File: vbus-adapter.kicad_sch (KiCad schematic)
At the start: 32 parts, among them J1 VBUS, J2 CAN, J3 Screw_Terminal_01x03, J4 Screw_Terminal_01x03, J6 Backup GPIO, T800 AO3400A, U1 ISO7721D, U3 MCP2562-E-SN, U4 WeMos_S2_mini

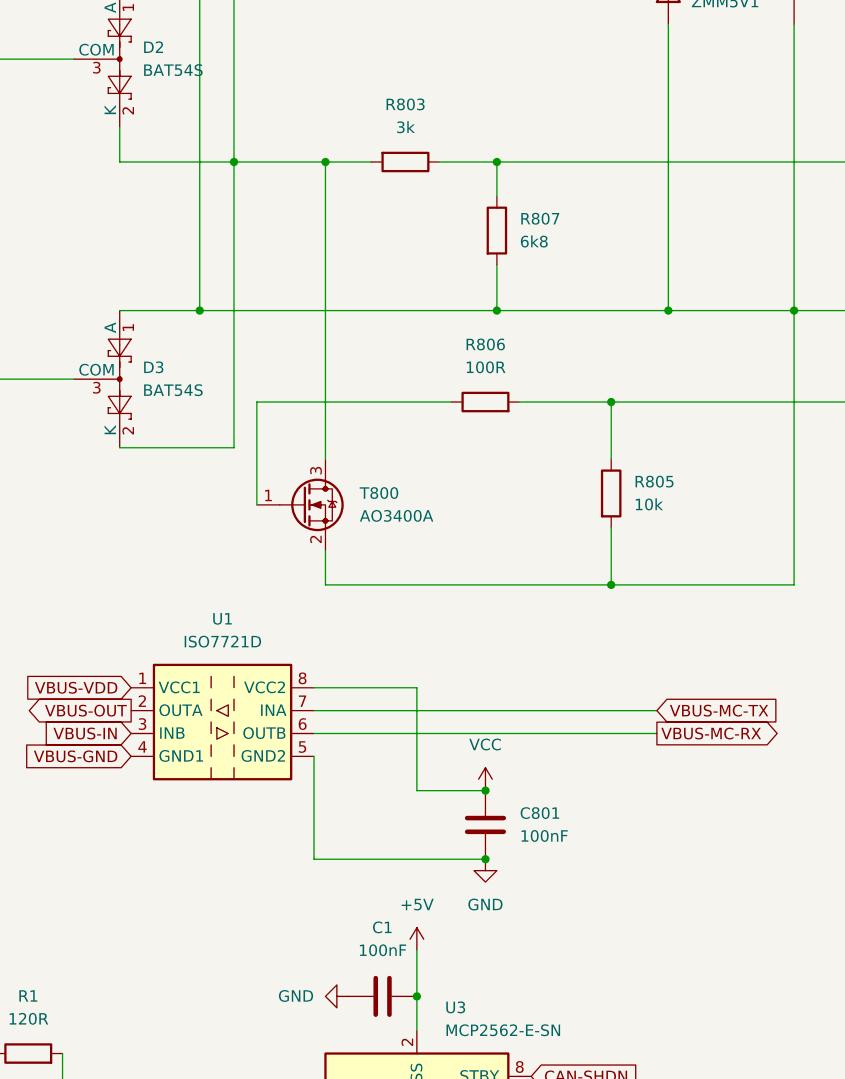
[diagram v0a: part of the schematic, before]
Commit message: Fix some issues
- Use ISO7721FDR (Default Low output) so on disconnect of
  the ESP32 (Power loss) the VBUS will not be pulled to low
  e.g. bus disabled.
- Add pull-down resistor to ISO input for TX
- Add VBUS r/w jumper disconnecting the MOSFet drain from the VBUS
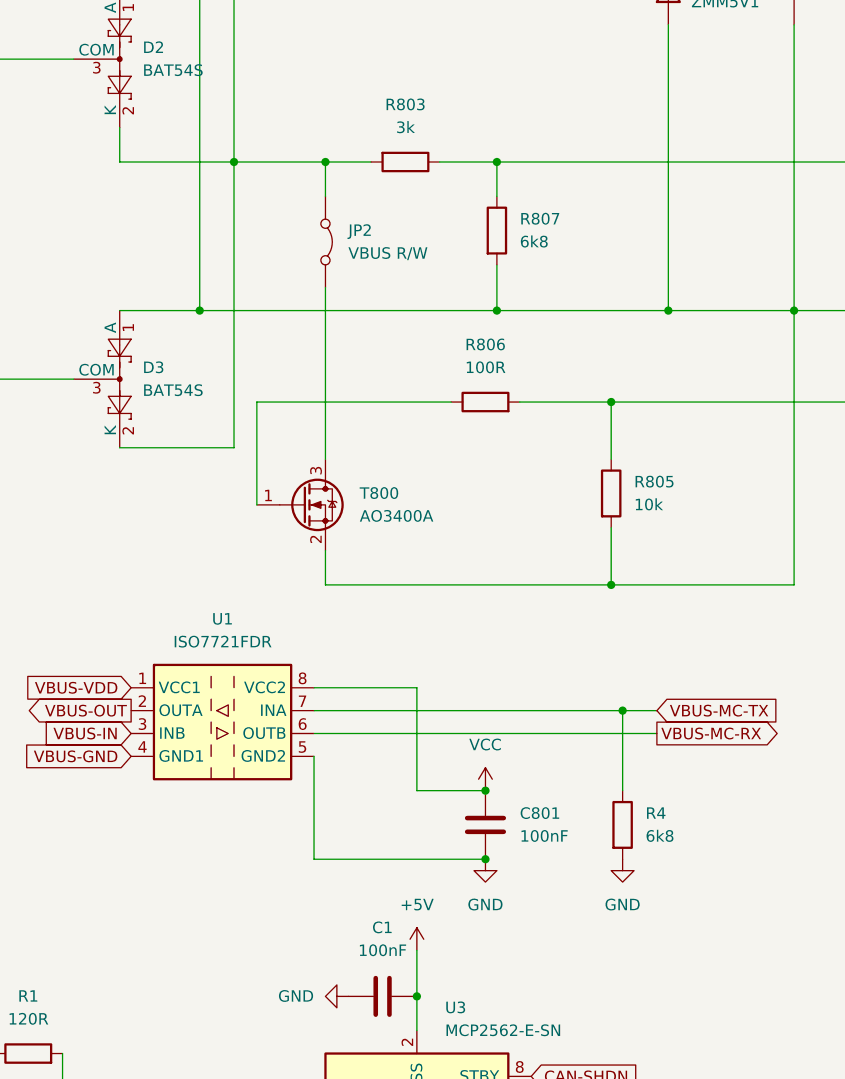
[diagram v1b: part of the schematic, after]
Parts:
- added JP2: VBUS R/W, Connector_PinHeader_2.54mm:PinHeader_1x02_P2.54mm_Vertical, symbol Jumper:Jumper_2_Bridged
- added R4: 6k8, Resistor_SMD:R_0805_2012Metric_Pad1.20x1.40mm_HandSolder, symbol Device:R
- U1: value ISO7721D -> ISO7721FDR
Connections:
- net GND: now also R4.2
- net VBUS-MC-TX: now also R4.1
- net at D2.2 (K), D3.2 (K), D4.3 (COM)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: now also JP2.1 (A); no longer T800.3 (D)
- new net: JP2.2 (B), T800.3 (D)
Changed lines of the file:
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@@
 	)
 	(junction
+		(at 137.16 119.38)
+		(diameter 0)
+		(color 0 0 0 0)
+	)
+	(junction
 		(at 54.61 162.56)
 		(diameter 0)
@@
 	(wire
 		(pts
+			(xy 104.14 72.39) (xy 104.14 91.44)
+		)
+		(stroke
+			(width 0)
+			(type default)
+		)
+	)
+	(wire
+		(pts
 			(xy 104.14 58.42) (xy 109.22 58.42)
 		)
@@
 	(wire
 		(pts
+			(xy 137.16 119.38) (xy 140.97 119.38)
+		)
+		(stroke
+			(width 0)
+			(type default)
+		)
+	)
+	(wire
+		(pts
 			(xy 171.45 43.18) (xy 171.45 74.93)
 		)
@@
 	(wire
 		(pts
-			(xy 104.14 58.42) (xy 104.14 91.44)
+			(xy 104.14 58.42) (xy 104.14 62.23)
 		)
 		(stroke
@@
 	(wire
 		(pts
+			(xy 137.16 128.27) (xy 137.16 119.38)
+		)
+		(stroke
+			(width 0)
+			(type default)
+		)
+	)
+	(wire
+		(pts
 			(xy 156.21 29.21) (xy 171.45 29.21)
 		)
@@
 	(wire
 		(pts
-			(xy 102.87 119.38) (xy 140.97 119.38)
+			(xy 102.87 119.38) (xy 137.16 119.38)
 		)
 		(stroke
@@
 	)
 	(symbol
+		(lib_id "power:GND")
+		(at 137.16 135.89 0)
+		(unit 1)
+		(exclude_from_sim no)
+		(in_bom yes)
+		(on_board yes)
+		(dnp no)
+		(fields_autoplaced yes)
+		(property "Reference" "#PWR015"
+			(at 137.16 142.24 0)
+			(effects
+				(font
+					(size 1.27 1.27)
+				)
+				(hide yes)
+			)
+		)
+		(property "Value" "GND"
+			(at 137.16 140.97 0)
+			(effects
+				(font
+					(size 1.27 1.27)
+				)
+			)
+		)
+		(property "Footprint" ""
+			(at 137.16 135.89 0)
+			(effects
+				(font
+					(size 1.27 1.27)
+				)
+				(hide yes)
+			)
+		)
+		(property "Datasheet" ""
+			(at 137.16 135.89 0)
+			(effects
+				(font
+					(size 1.27 1.27)
+				)
+				(hide yes)
+			)
+		)
+		(property "Description" "Power symbol creates a global label with name \"GND\" , ground"
+			(at 137.16 135.89 0)
+			(effects
+				(font
+					(size 1.27 1.27)
+				)
+				(hide yes)
+			)
+		)
+		(pin "1"
+		)
+		(instances
+			(project "vbus-adapter"
+				(path "/c5b76d16-c954-491e-a7b2-87b879d4d4be"
+					(reference "#PWR015")
+					(unit 1)
+				)
+			)
+		)
+	)
+	(symbol
 		(lib_id "Diode:SMAJ12CA")
 		(at 55.88 63.5 270)
@@
 			)
 		)
-		(property "Value" "ISO7721D"
+		(property "Value" "ISO7721FDR"
 			(at 92.71 111.76 0)
 			(effects
@@
 	)
 	(symbol
+		(lib_id "Jumper:Jumper_2_Bridged")
+		(at 104.14 67.31 270)
+		(unit 1)
+		(exclude_from_sim no)
+		(in_bom yes)
+		(on_board yes)
+		(dnp no)
+		(fields_autoplaced yes)
+		(property "Reference" "JP2"
+			(at 106.68 66.0399 90)
+			(effects
+				(font
+					(size 1.27 1.27)
+				)
+				(justify left)
+			)
+		)
+		(property "Value" "VBUS R/W"
+			(at 106.68 68.5799 90)
+			(effects
+				(font
+					(size 1.27 1.27)
+				)
+				(justify left)
+			)
+		)
+		(property "Footprint" "Connector_PinHeader_2.54mm:PinHeader_1x02_P2.54mm_Vertical"
+			(at 104.14 67.31 0)
+			(effects
+				(font
+					(size 1.27 1.27)
+				)
+				(hide yes)
+			)
+		)
+		(property "Datasheet" "~"
+			(at 104.14 67.31 0)
+			(effects
+				(font
+					(size 1.27 1.27)
+				)
+				(hide yes)
+			)
+		)
+		(property "Description" "Jumper, 2-pole, closed/bridged"
+			(at 104.14 67.31 0)
+			(effects
+				(font
+					(size 1.27 1.27)
+				)
+				(hide yes)
+			)
+		)
+		(pin "2"
+		)
+		(pin "1"
+		)
+		(instances
+			(project "vbus-adapter"
+				(path "/c5b76d16-c954-491e-a7b2-87b879d4d4be"
+					(reference "JP2")
+					(unit 1)
+				)
+			)
+		)
+	)
+	(symbol
 		(lib_id "Diode:BAT54S")
 		(at 101.6 21.59 270)
@@
 					(unit 1)
 				)
+			)
+		)
+	)
+	(symbol
+		(lib_id "Device:R")
+		(at 137.16 132.08 0)
+		(unit 1)
+		(exclude_from_sim no)
+		(in_bom yes)
+		(on_board yes)
+		(dnp no)
+		(fields_autoplaced yes)
+		(property "Reference" "R4"
+			(at 139.7 130.8099 0)
+			(effects
+				(font
+					(size 1.27 1.27)
+				)
+				(justify left)
+			)
+		)
+		(property "Value" "6k8"
+			(at 139.7 133.3499 0)
+			(effects
+				(font
+					(size 1.27 1.27)
+				)
+				(justify left)
+			)
+		)
+		(property "Footprint" "Resistor_SMD:R_0805_2012Metric_Pad1.20x1.40mm_HandSolder"
+			(at 135.382 132.08 90)
+			(effects
+				(font
+					(size 1.27 1.27)
+				)
+				(hide yes)
+			)
+		)
+		(property "Datasheet" "~"
+			(at 137.16 132.08 0)
+			(effects
+				(font
+					(size 1.27 1.27)
+				)
+				(hide yes)
+			)
+		)
+		(property "Description" "Resistor"
+			(at 137.16 132.08 0)
+			(effects
+				(font
+					(size 1.27 1.27)
+				)
+				(hide yes)
+			)
+		)
+		(pin "2"
+		)
+		(pin "1"
+		)
+		(instances
+			(project "vbus-adapter"
+				(path "/c5b76d16-c954-491e-a7b2-87b879d4d4be"
+					(reference "R4")
+					(unit 1)
+				)

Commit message: Version 2
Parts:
- removed U4: WeMos_S2_mini, flo:WEMOS_S2_mini, symbol WEMOS_S2_mini:WeMos_S2_mini
- added C3, C6: 10uF, Capacitor_SMD:C_0805_2012Metric_Pad1.18x1.45mm_HandSolder, symbol Device:C_Polarized
- added C4, C5: 0.1uF, Capacitor_SMD:C_0805_2012Metric_Pad1.18x1.45mm_HandSolder, symbol Device:C
- added C7: 10nF, Capacitor_SMD:C_0805_2012Metric_Pad1.18x1.45mm_HandSolder, symbol Device:C
- added J5: Power, TerminalBlock_Phoenix:TerminalBlock_Phoenix_MPT-0,5-2-2.54_1x02_P2.54mm_Horizontal, symbol Connector:Screw_Terminal_01x02
- added J7: Program, Connector_PinHeader_2.54mm:PinHeader_1x05_P2.54mm_Vertical, symbol Connector:Conn_01x05_Pin
- added Q1, Q2: SS8050, Package_TO_SOT_SMD:SOT-23, symbol Transistor_BJT:SS8050
- added R5, R6: 10K, Resistor_SMD:R_0805_2012Metric_Pad1.20x1.40mm_HandSolder, symbol Device:R
- added U2: ESP32-S2-SOLO, PCM_Espressif:ESP32-S2-SOLO, symbol PCM_Espressif:ESP32-S2-SOLO
- added U5: SPX3819M5-L-3-3, Package_TO_SOT_SMD:SOT-23-5, symbol Regulator_Linear:SPX3819M5-L-3-3
- J1, J2: footprint TerminalBlock_Phoenix:TerminalBlock_Phoenix_MKDS-1,5-2-5.08_1x02_P5.08mm_Horizontal -> TerminalBlock_Phoenix:TerminalBlock_Phoenix_MPT-0,5-2-2.54_1x02_P2.54mm_Horizontal
- J3: value Screw_Terminal_01x03 -> Sens 2; footprint TerminalBlock_Phoenix:TerminalBlock_Phoenix_MKDS-1,5-3-5.08_1x03_P5.08mm_Horizontal -> TerminalBlock_Phoenix:TerminalBlock_Phoenix_MPT-0,5-3-2.54_1x03_P2.54mm_Horizontal
- J4: value Screw_Terminal_01x03 -> Sens 1; footprint TerminalBlock_Phoenix:TerminalBlock_Phoenix_MKDS-1,5-3-5.08_1x03_P5.08mm_Horizontal -> TerminalBlock_Phoenix:TerminalBlock_Phoenix_MPT-0,5-3-2.54_1x03_P2.54mm_Horizontal
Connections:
- net +5V: now also C3.1, C4.1, J5.1 (Pin_1), U5.1 (IN), U5.3 (EN)
- net CAN-RX: now also U2.12 (GPIO8/TOUCH8/ADC1_CH7)
- net CAN-SHDN: now also U2.4 (GPIO4/TOUCH4/ADC1_CH3)
- net CAN-TX: now also U2.6 (GPIO6/TOUCH6/ADC1_CH5)
- net GND: now also C3.2, C4.2, C5.2, C6.2, C7.2, J5.2 (Pin_2), J7.1 (Pin_1), U2.1 (GND), U2.40 (GND), U2.41 (GND), U5.2 (GND)
- net GPIO-SENS1: now also U2.26 (GPIO45)
- net GPIO-SENS2: now also U2.25 (SPIIO5/GPIO34/FSPICS0)
- net VBUS-MC-RX: now also U2.20 (GPIO12/TOUCH12/ADC2_CH1/FSPICLK/FSPIIO6)
- net VBUS-MC-TX: now also U2.19 (GPIO11/TOUCH11/ADC2_CH0/FSPID/FSPIIO5)
- net VCC: now also C5.1, C6.1, U2.2 (3V3), U5.5 (OUT)
- net GPIO3 renamed EXT4
- net EXT4: now also U2.33 (MTDO/GPIO40/CLK_OUT2)
- net GPIO5 renamed EXT3
- net EXT3: now also U2.32 (MTCK/GPIO39/CLK_OUT3)
- net GPIO7 renamed EXT2
- net EXT2: now also U2.31 (GPIO38/FSPIWP)
- net GPIO9 renamed EXT1
- net EXT1: now also U2.30 (SPIDQS/GPIO37/FSPIQ)
- new net: J7.4 (Pin_4), Q2.2 (E), R6.2
- new net: J7.5 (Pin_5), Q1.2 (E), R5.2
- new net: C7.1, U5.4 (BP)
- new net: Q1.1 (B), R6.1
- new net: Q2.1 (B), R5.1
- new net EN: Q1.3 (C), U2.3 (EN)
- new net PROG: Q2.3 (C), U2.27 (GPIO0)
- new net PROG_RXD: J7.2 (Pin_2), U2.36 (U0RXD/GPIO44/CLK_OUT2)
- new net PROG_TXD: J7.3 (Pin_3), U2.37 (U0TXD/GPIO43/CLK_OUT1)
- no-connect marks 18 -> 23
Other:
- title: (none) -> vbus-adapter

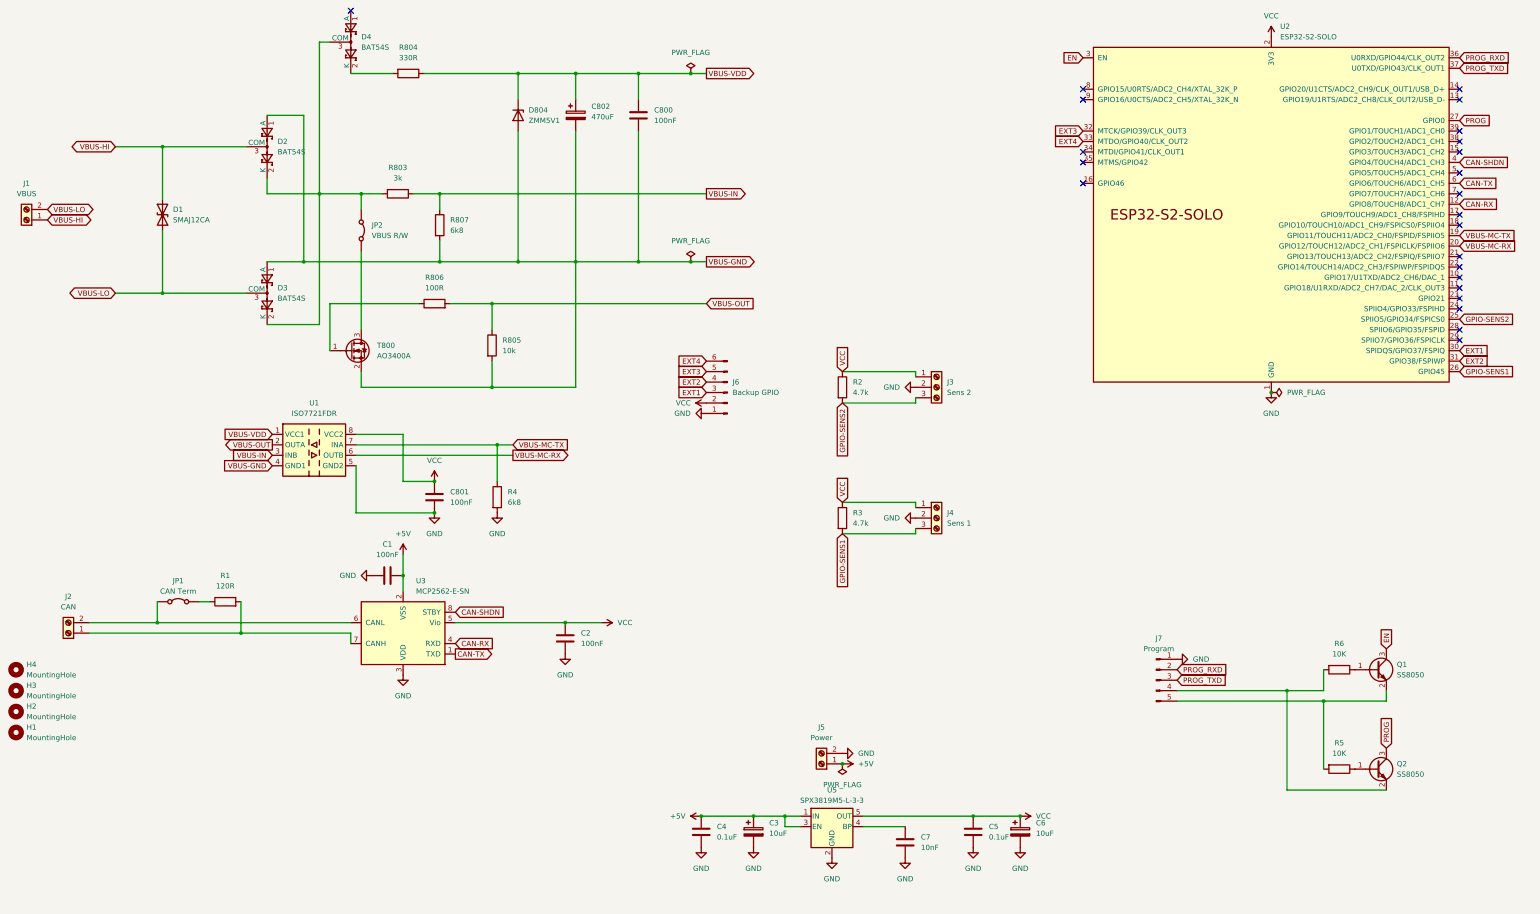
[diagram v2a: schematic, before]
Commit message: Version 3 - Move GPIO for SENS, Add PWR/WIFI LED
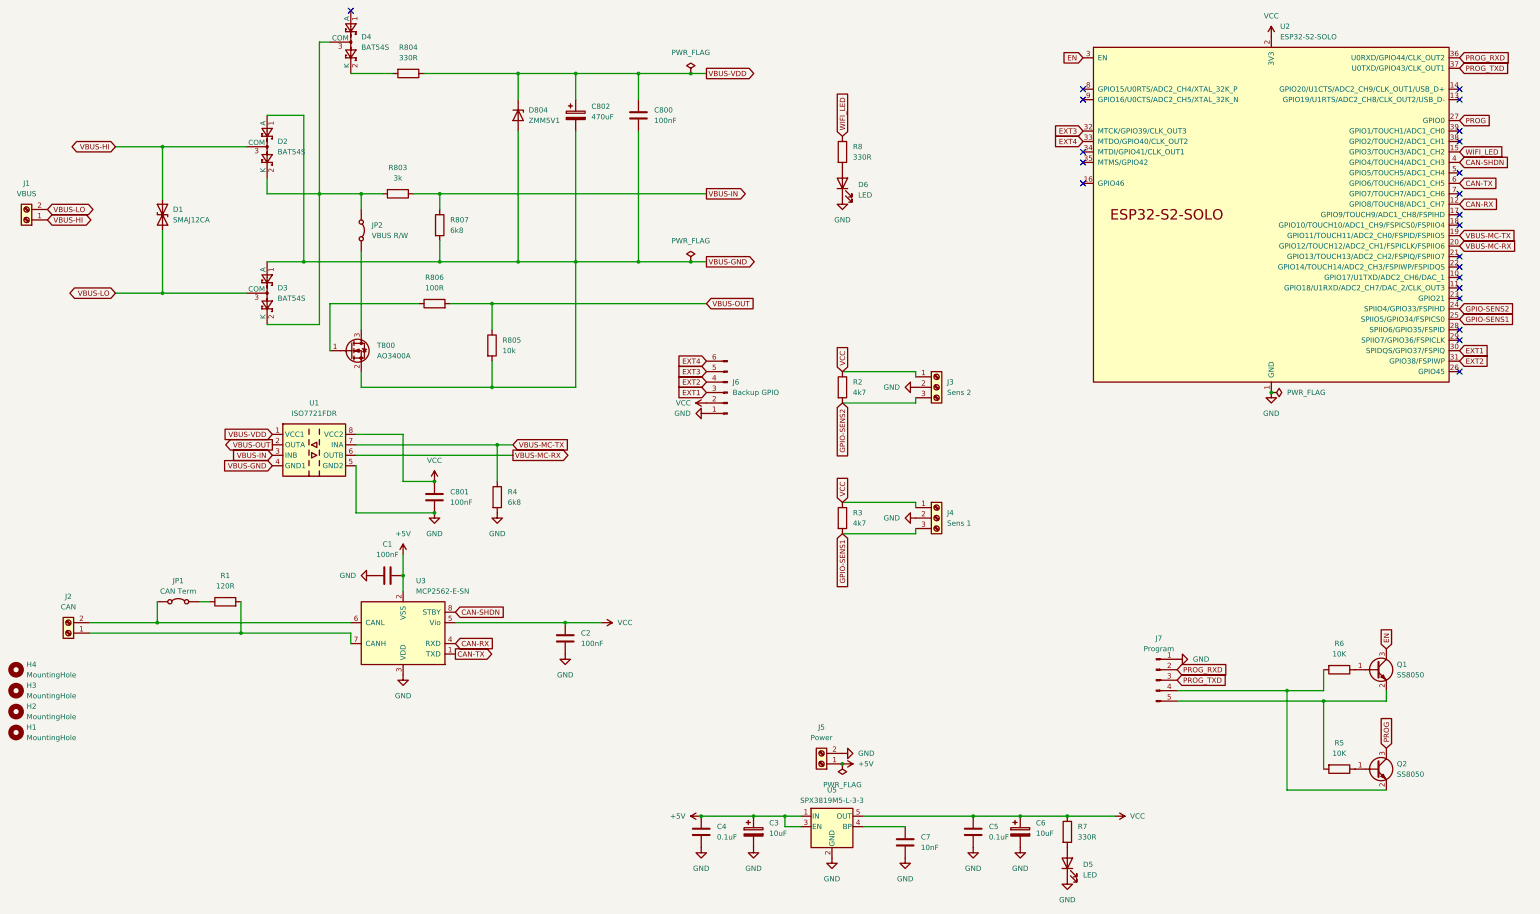
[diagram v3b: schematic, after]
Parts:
- added D5, D6: LED, LED_SMD:LED_0805_2012Metric_Pad1.15x1.40mm_HandSolder, symbol Device:LED
- added R7, R8: 330R, Resistor_SMD:R_0805_2012Metric_Pad1.20x1.40mm_HandSolder, symbol Device:R
- R2, R3: value 4.7k -> 4k7
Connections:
- net GND: now also D5.1 (K), D6.1 (K)
- net GPIO-SENS1: now also U2.25 (SPIIO5/GPIO34/FSPICS0); no longer U2.26 (GPIO45)
- net GPIO-SENS2: now also U2.24 (SPIIO4/GPIO33/FSPIHD); no longer U2.25 (SPIIO5/GPIO34/FSPICS0)
- net VCC: now also R7.1
- net WIFI_LED: now reaches U2.15 (GPIO3/TOUCH3/ADC1_CH2)
- net WIFI_LED: now also R8.1
- new net: D5.2 (A), R7.2
- new net: D6.2 (A), R8.2
- no-connect marks 23 -> 22
